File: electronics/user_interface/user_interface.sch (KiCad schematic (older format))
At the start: 66 parts, among them J1 Conn_01x06, J2 Conn_02x05_Odd_Even, SW1 ALPS_EC11E18244A5, U1 PCF8574, U2 PCF8574

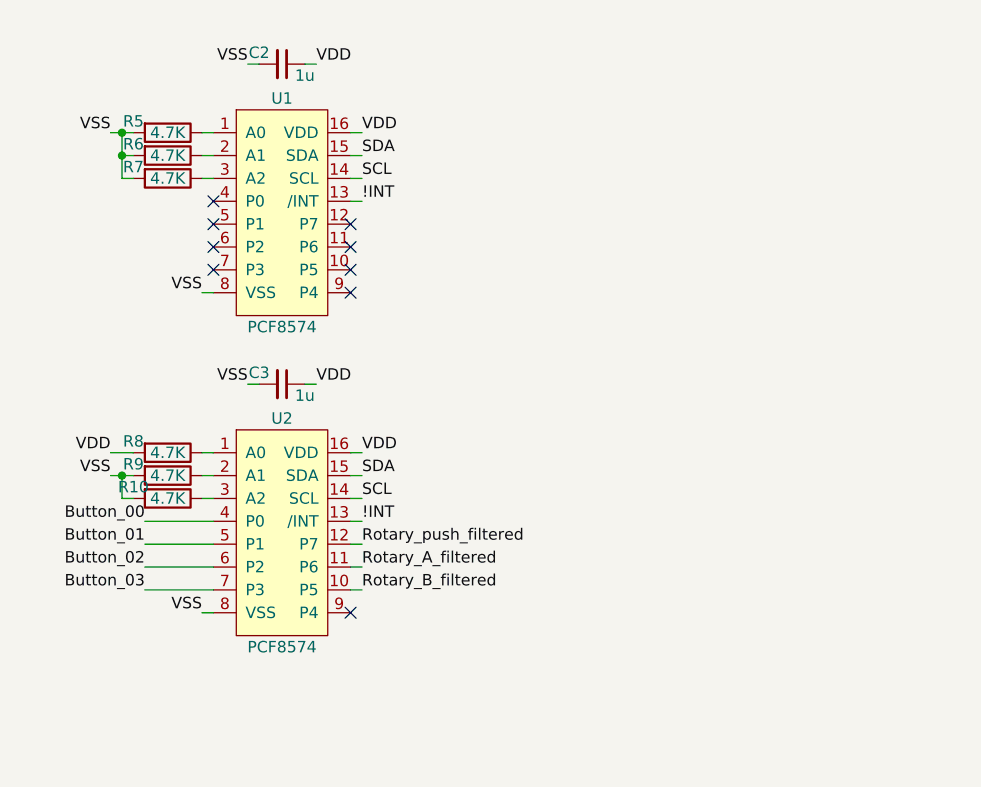
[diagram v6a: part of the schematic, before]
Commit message: Added LCD, connections to expander and LCD bias circuit
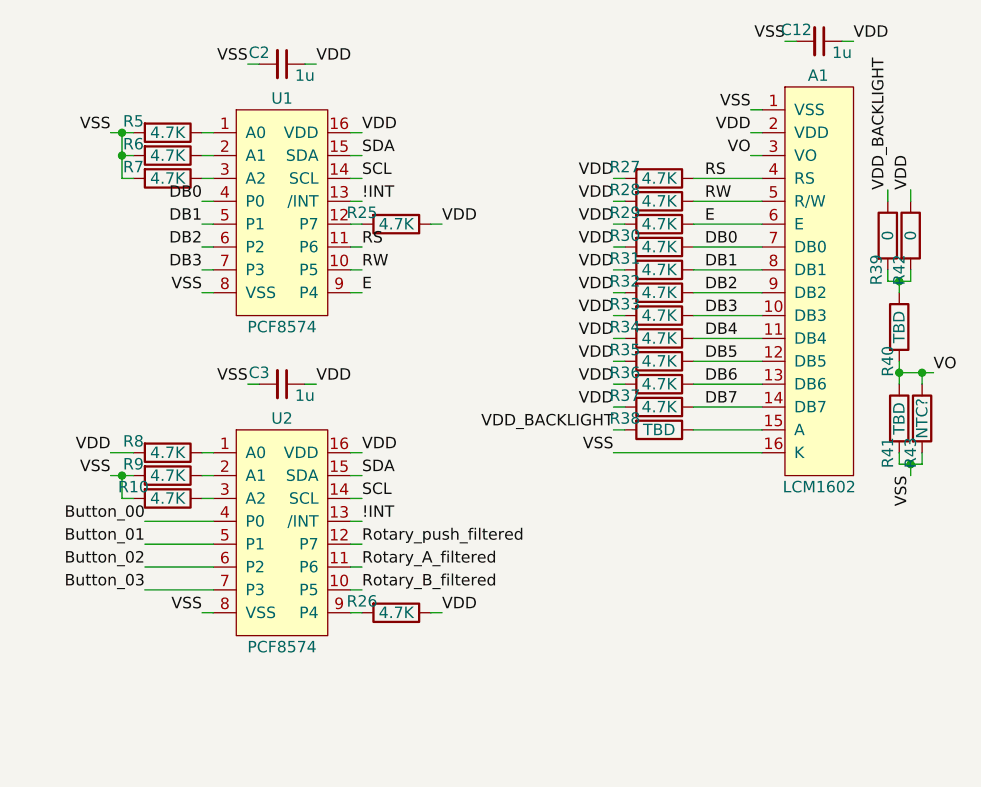
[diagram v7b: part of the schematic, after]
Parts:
- added A1: LCM1602, SquantorModules:LCM1602K, symbol SquantorModules:LCM1602
- added C12: 1u, SquantorRcl:C_0603, symbol Device:C_Small
- added R25, R26, R27, R28, R29, R30, R31, R32, R33, R34, R35, R36, R37: 4.7K, SquantorRcl:R_0603_hand, symbol Device:R
- added R38, R40, R41: TBD, SquantorRcl:R_0603_hand, symbol Device:R
- added R39, R42: 0, SquantorRcl:R_0603_hand, symbol Device:R
- added R43: NTC?, SquantorRcl:R_0603_hand, symbol Device:R
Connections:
- net VDD: now also A1.2 (VDD), C12.1, R25.1, R26.1, R27.2, R28.2, R29.2, R30.2, R31.2, R32.2, R33.2, R34.2, R35.2, R36.2, R37.2, R42.1
- net VDD_BACKLIGHT: now also R38.2, R39.1
- net VSS: now also A1.1 (VSS), A1.16 (K), C12.2, R41.2, R43.2
- net RW: now reaches U1.10 (P5)
- net RW: now also A1.5 (R/W), R28.1
- net RS: now reaches U1.11 (P6)
- net RS: now also A1.4 (RS), R27.1
- net at U1.12 (P7): now also R25.2
- net DB0: now reaches U1.4 (P0)
- net DB0: now also A1.7 (DB0), R30.1
- net DB1: now reaches U1.5 (P1)
- net DB1: now also A1.8 (DB1), R31.1
- net DB2: now reaches U1.6 (P2)
- net DB2: now also A1.9 (DB2), R32.1
- net DB3: now reaches U1.7 (P3)
- net DB3: now also A1.10 (DB3), R33.1
- net E: now reaches U1.9 (P4)
- net E: now also A1.6 (E), R29.1
- net at U2.9 (P4): now also R26.2
- new net: A1.15 (A), R38.1
- new net: R39.2, R40.1, R42.2
- new net DB4: A1.11 (DB4), R34.1
- new net DB5: A1.12 (DB5), R35.1
- new net DB6: A1.13 (DB6), R36.1
- new net DB7: A1.14 (DB7), R37.1
- new net VO: A1.3 (VO), R40.2, R41.1, R43.1
- no-connect marks 9 -> 0

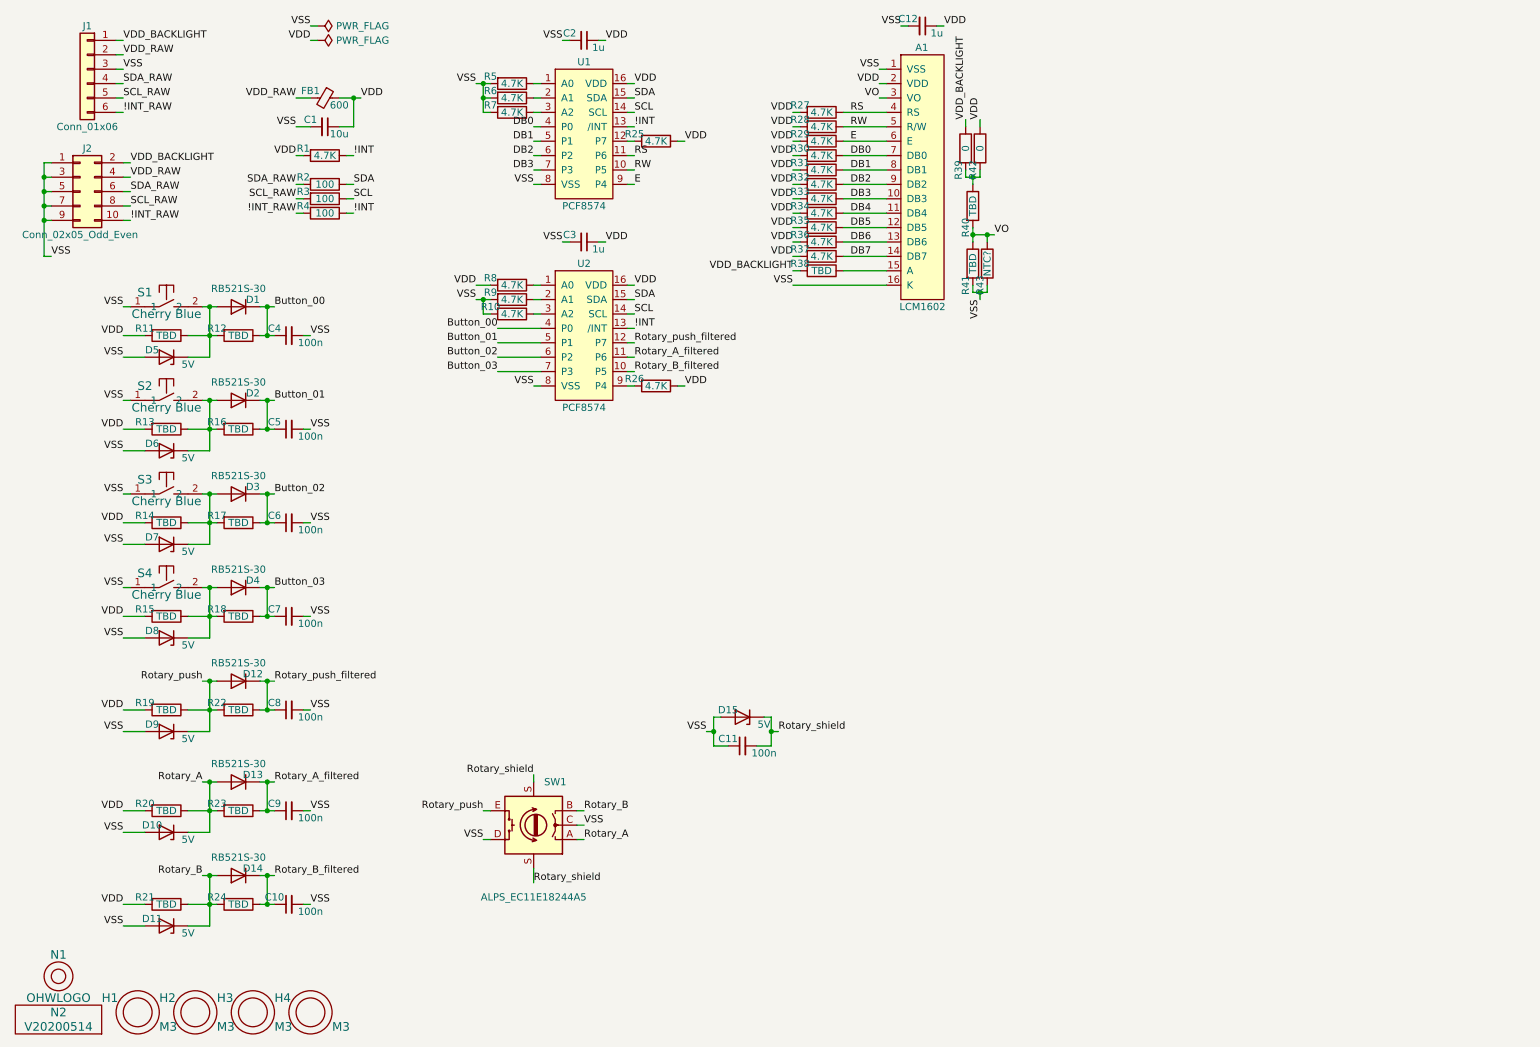
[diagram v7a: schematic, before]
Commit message: beautified schematic a bit, passes ERC
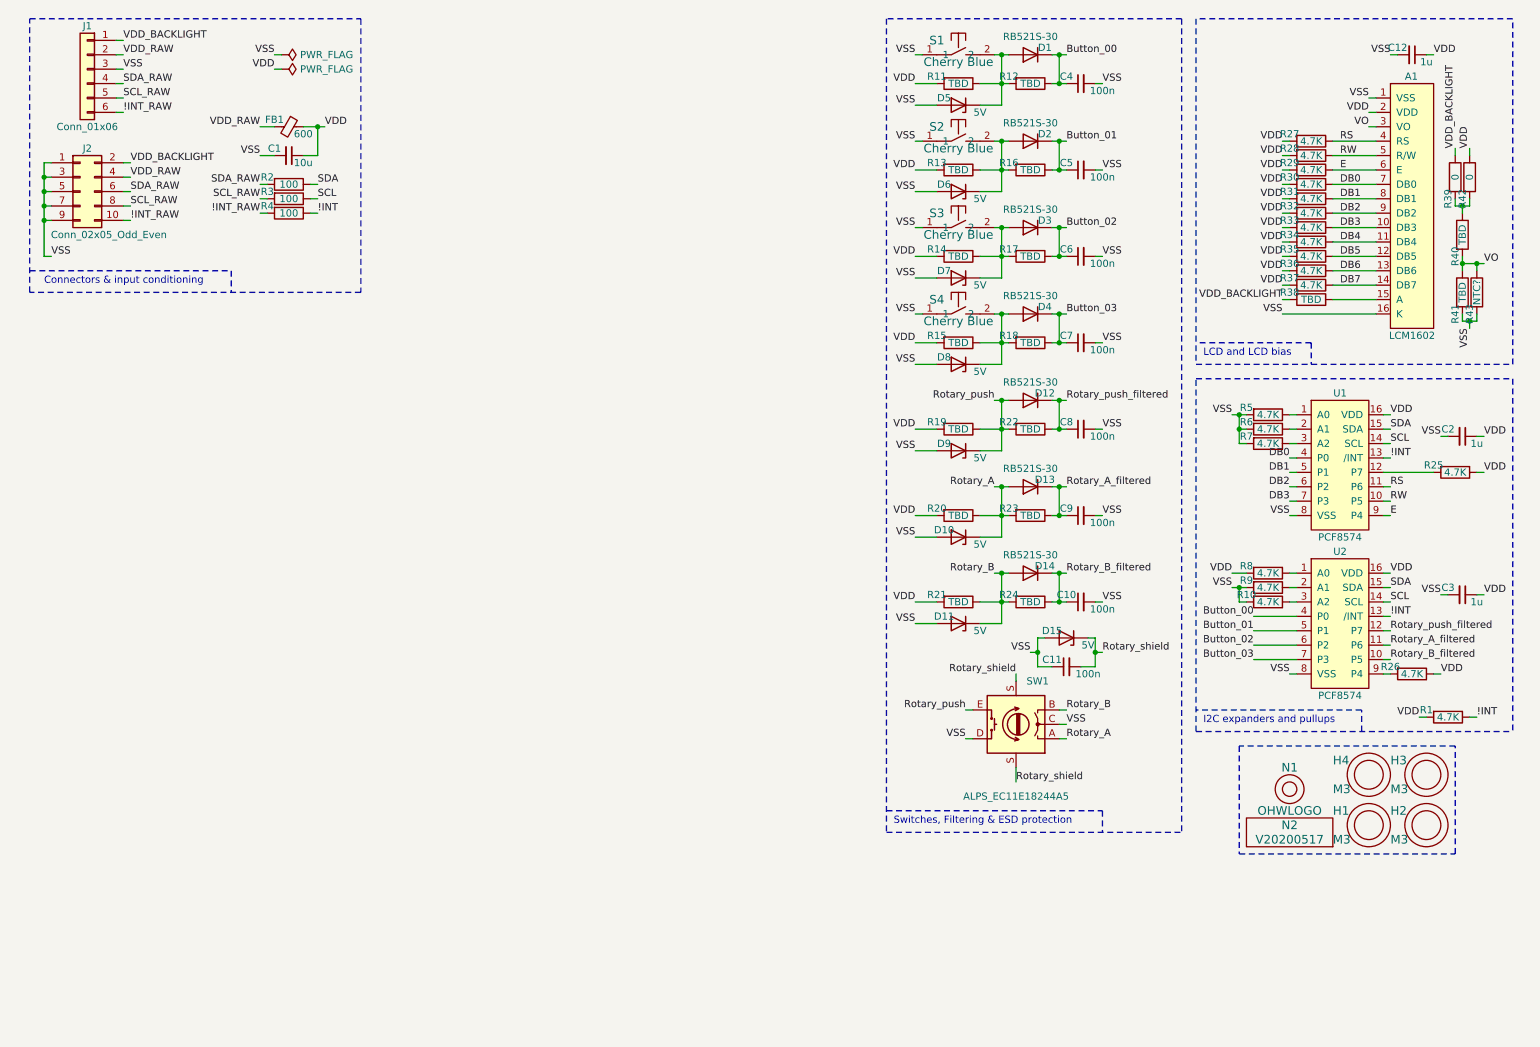
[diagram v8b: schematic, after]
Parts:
- N2: value V20200514 -> V20200517; footprint SquantorLabels:Label_version -> SquantorLabels:Label_Generic
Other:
- note added: "Connectors & input conditioning"
- note added: "I2C expanders and pullups"
- note added: "LCD and LCD bias"
- note added: "Switches, Filtering & ESD protection"
- moved on the sheet: A1, C1, C10, C11, C12, C2, C3, C4, C5, C6, C7, C8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
